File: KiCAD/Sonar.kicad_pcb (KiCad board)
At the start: 4 copper layers, 100 x 100 mm, 16 parts, among them U2 LM1875, U3 LM1875

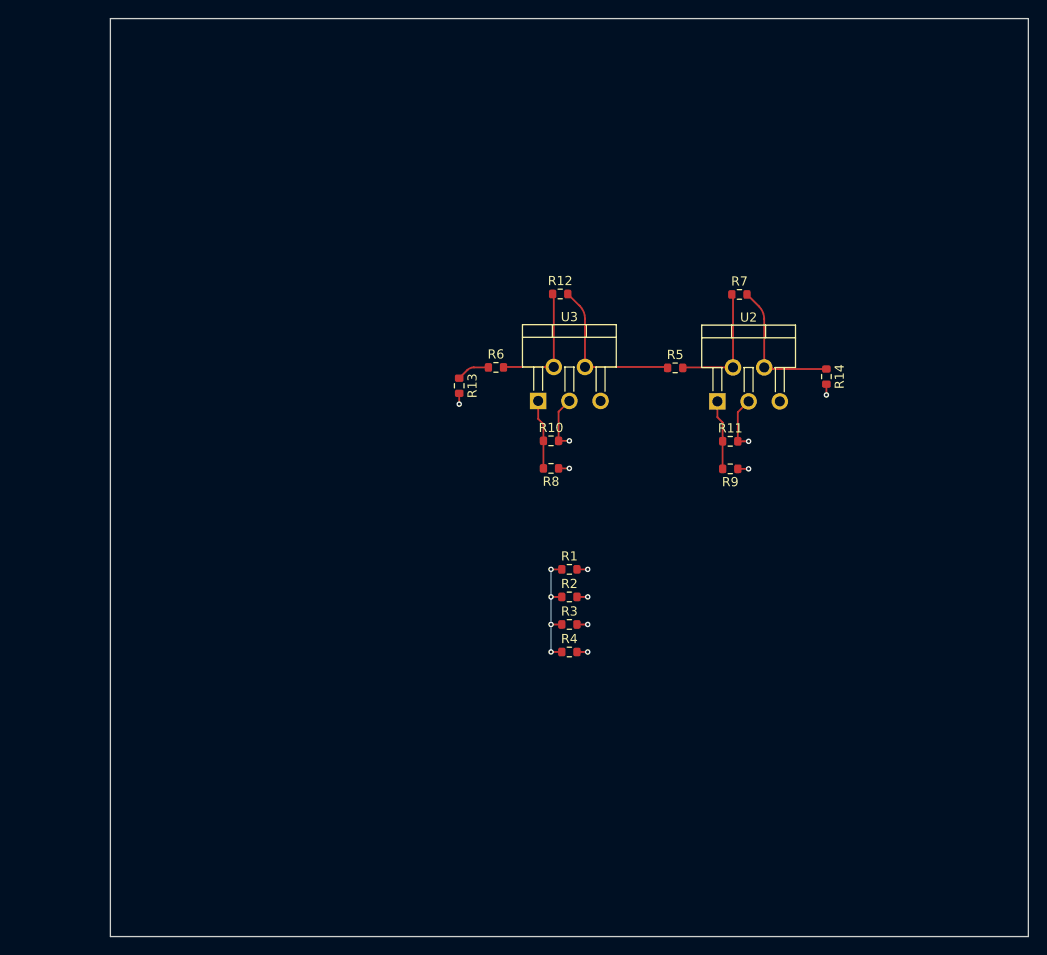
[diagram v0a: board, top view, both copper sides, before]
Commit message: Completed the schematic
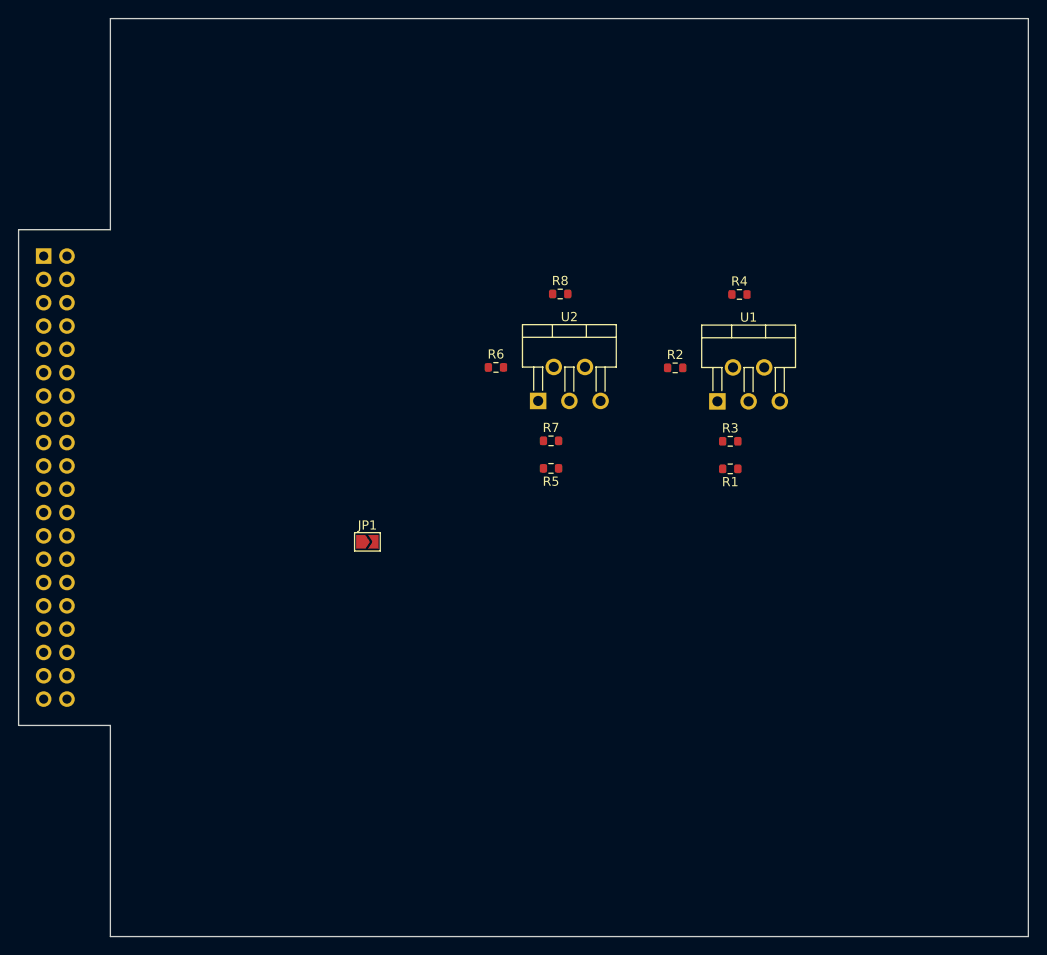
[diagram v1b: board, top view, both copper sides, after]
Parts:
- removed the R1 at (150.0, 110.0)
- removed R13, R14: 1k, Resistor_SMD:R_0603_1608Metric
- removed the R2 at (150.0, 113.0)
- removed the R3 at (150.0, 116.0)
- removed the R4 at (150.0, 119.0)
- added J1: DIN-40-Female, Connector_PinSocket_2.54mm:PinSocket_2x20_P2.54mm_Vertical, B.Cu at (92.7, 75.9)
- added JP1: SolderJumper_2_Open, Jumper:SolderJumper-2_P1.3mm_Open_TrianglePad1.0x1.5mm, F.Cu at (128.0, 107.0)
- renumbered R9 to R1, R5 to R2, R11 to R3, R7 to R4, R8 to R5, R10 to R7, R12 to R8, U2 to U1, U3 to U2
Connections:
- R8 pad 2: /Power/Input -> /Transducers/Output
- U2 pad 4: /Power/Input -> /Transducers/Output
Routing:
- net GND: track 19.1 -> 0.00 mm, vias 8 -> 0
- net /Power/Input: track 17.7 -> 0.00 mm
- net /Power/Output: track 15.5 -> 0.00 mm
- net Net-(R1-Pad1): track 13.7 -> 0.00 mm, vias 4 -> 0
- net Net-(U2--): track 13.5 -> 0.00 mm
- net Net-(U1--): track 13.5 -> 0.00 mm
- net Net-(U2-+): track 7.59 -> 0.00 mm
- net Net-(U1-+): track 7.59 -> 0.00 mm
- net /Transducers/Input: track 3.61 -> 0.00 mm
- net +5V: track 2.35 -> 0.00 mm, vias 2 -> 0
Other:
- board size 100 x 100 mm -> 110 x 100 mm
